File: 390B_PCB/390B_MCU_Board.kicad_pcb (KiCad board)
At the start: 2 copper layers, 78 x 80 mm, 17 parts, among them J1 Programmer Connector, J3 Motor Pins, J4 Photo R Pins, U1 ATMEGA328-PU

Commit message: Fixed Chase's Fatal Mistake
The PCB no longer shorts the battery
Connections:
- R2 pad 1: GND -> /Vbatt
- U2 pad 1: GND -> /Vbatt
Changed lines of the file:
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@@
 	(net 32 "unconnected-(U3-PGOOD-Pad6)")
 	(net 33 "unconnected-(U3-OUT-Pad8)")
+	(net 34 "/Vbatt")
 	(footprint "Resistor_THT:R_Axial_DIN0207_L6.3mm_D2.5mm_P5.08mm_Vertical"
 		(layer "F.Cu")
@@
 			(layers "*.Cu" "*.Mask")
 			(remove_unused_layers no)
-			(net 1 "GND")
+			(net 34 "/Vbatt")
 			(pinfunction "Bat")
 			(pintype "bidirectional")
@@
 			(layers "*.Cu" "*.Mask")
 			(remove_unused_layers no)
-			(net 1 "GND")
+			(net 34 "/Vbatt")
 			(pintype "passive")
 		)

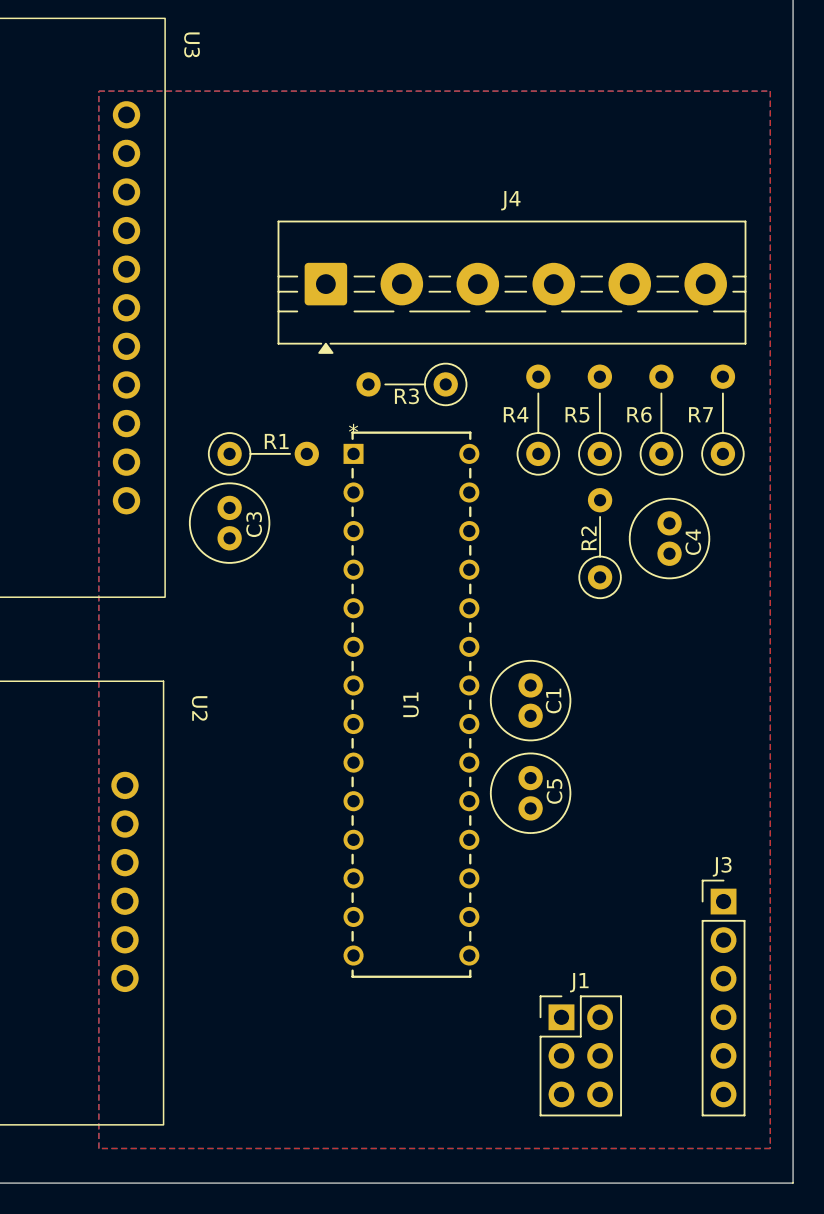
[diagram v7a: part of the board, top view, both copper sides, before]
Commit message: PCB Traced
All items connected on PCB, just a few silkscreen overlap errors need to be resolved.
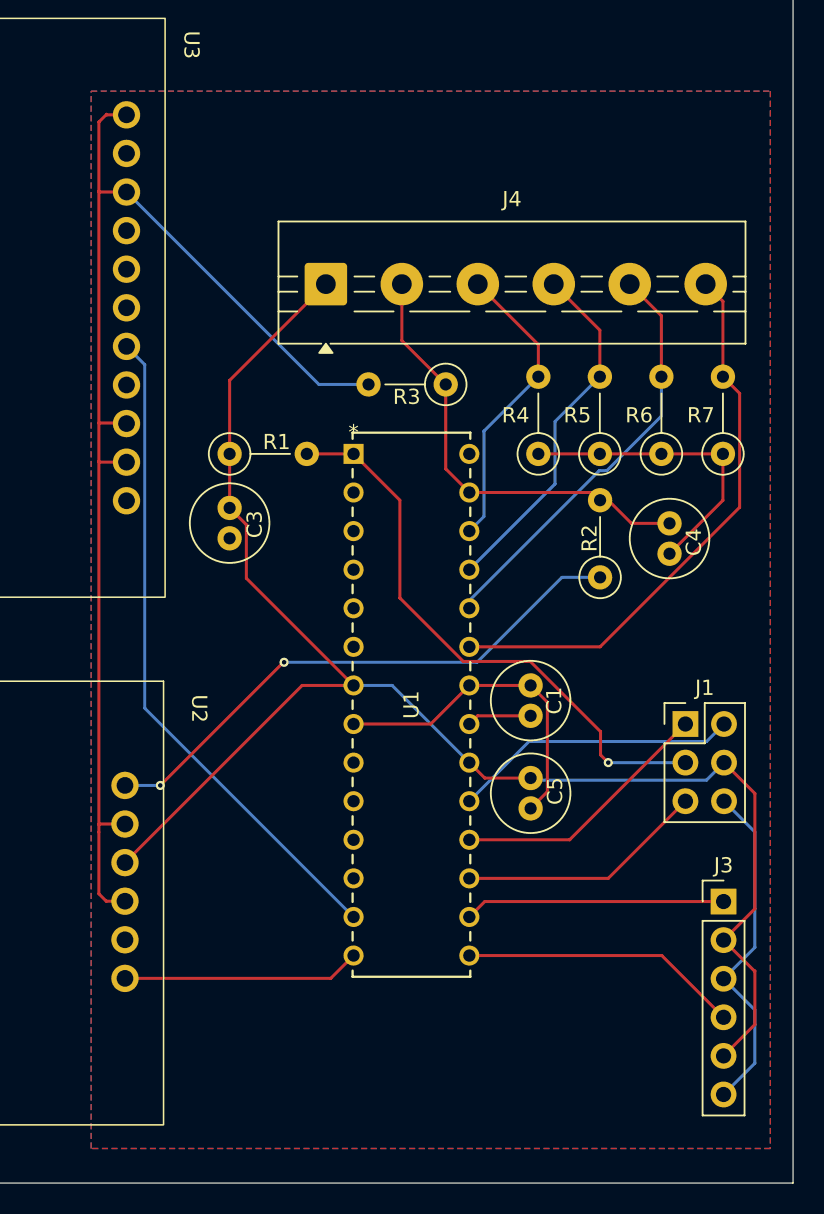
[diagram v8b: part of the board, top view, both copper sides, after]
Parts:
- moved J1 21.0 mm to (138.2, 98.0)
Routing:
- net GND: track 0.00 -> 147.8 mm
- net /VCC: track 0.00 -> 102.5 mm
- net /charge en: track 0.00 -> 43.7 mm
- net /RESET: track 0.00 -> 38.0 mm, vias 0 -> 1
- net /PhotoR0: track 0.00 -> 37.2 mm
- net /Vbatt: track 0.00 -> 37.0 mm, vias 0 -> 2
- net /batt v read: track 0.00 -> 29.6 mm
- net /PhotoR1: track 0.00 -> 27.7 mm
- net /PhotoR2: track 0.00 -> 23.6 mm
- net /PhotoR3: track 0.00 -> 20.3 mm
- net /SCK: track 0.00 -> 18.9 mm
- net /Motor 1: track 0.00 -> 18.4 mm
- net /MISO: track 0.00 -> 17.4 mm
- net /Motor 2: track 0.00 -> 17.2 mm
- net /MOSI: track 0.00 -> 16.3 mm
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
